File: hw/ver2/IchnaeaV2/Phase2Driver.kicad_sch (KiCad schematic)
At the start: 21 parts, among them Q2 MCAC80N10Y, Q3 MCAC80N10Y, Q4 MCAC80N10Y, Q5 MCAC80N10Y, U2 HIP2210

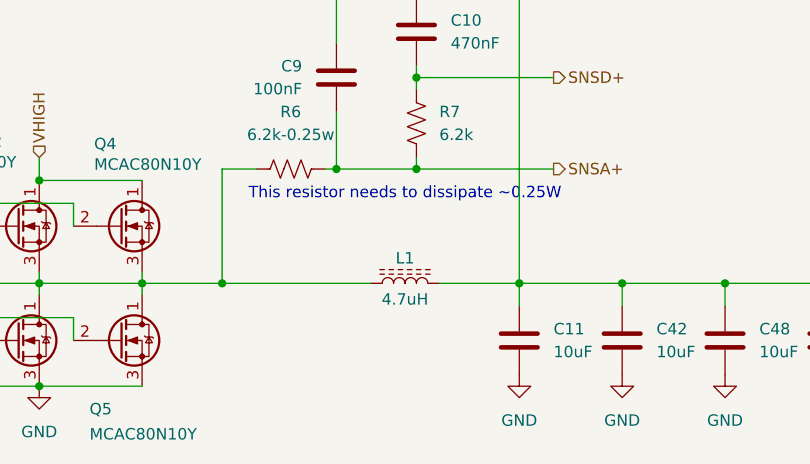
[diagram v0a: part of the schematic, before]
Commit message: Trying to optimize the high power loop area
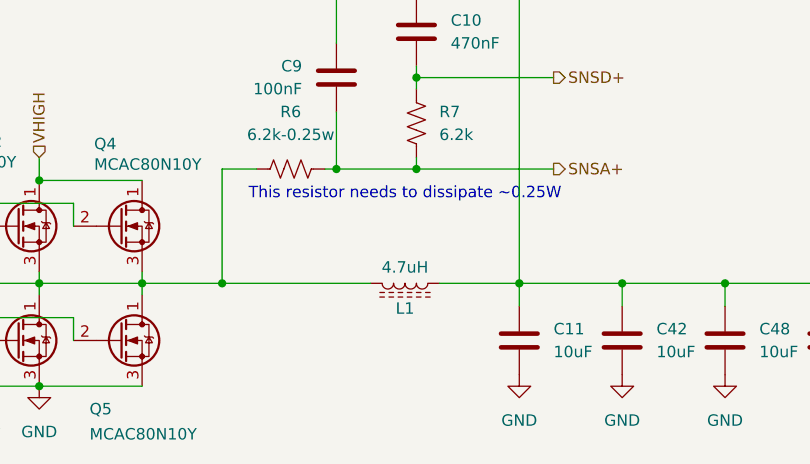
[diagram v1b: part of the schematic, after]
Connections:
- net SNSD-: now also L1.1; no longer L1.2
- net at C8.2, Q2.3 (S), Q3.1 (D)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: now also L1.2; no longer L1.1
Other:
- moved on the sheet: L1
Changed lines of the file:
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@@
 	(symbol
 		(lib_id "Device:L_Ferrite")
-		(at 203.2 95.25 90)
+		(at 203.2 95.25 270)
 		(unit 1)
 		(exclude_from_sim no)
@@
 		(dnp no)
 		(property "Reference" "L1"
-			(at 203.2 92.456 90)
+			(at 203.2 98.044 90)
 			(effects
 				(font
@@
 		)
 		(property "Value" "4.7uH"
-			(at 203.2 97.028 90)
+			(at 203.2 93.472 90)
 			(effects
 				(font
@@
 		)
 		(property "Digikey" "PQ2614BLA-3R3K-ND"
-			(at 203.708 99.06 90)
+			(at 202.692 91.44 90)
 			(effects
 				(font

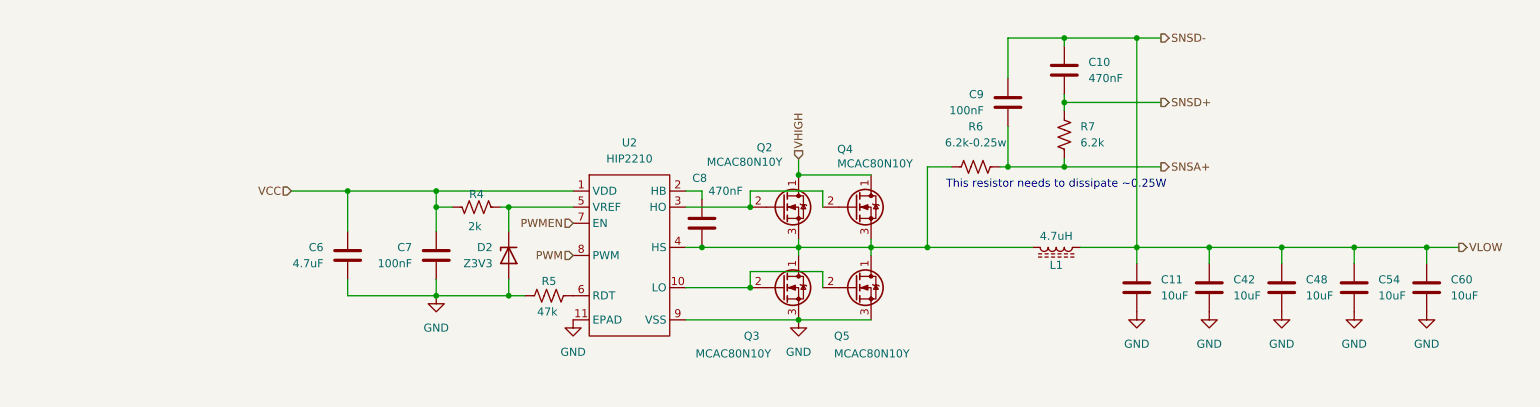
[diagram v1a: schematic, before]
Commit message: Trying to further compress power loop area
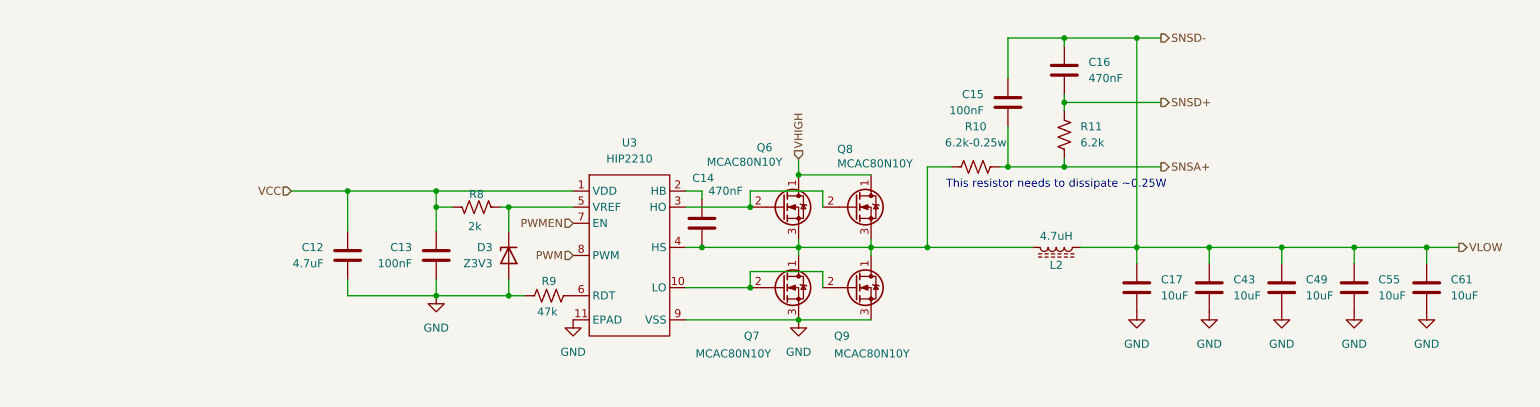
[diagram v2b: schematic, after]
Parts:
- renumbered C6 to C12, C7 to C13, C8 to C14, C9 to C15, C10 to C16, C11 to C17, C42 to C43, C48 to C49, C54 to C55, C60 to C61, D2 to D3, L1 to L2, Q2 to Q6, Q3 to Q7, Q4 to Q8, Q5 to Q9, R6 to R10, R7 to R11, R4 to R8, R5 to R9, U2 to U3

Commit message: Not quite happy with the power stage just yet.
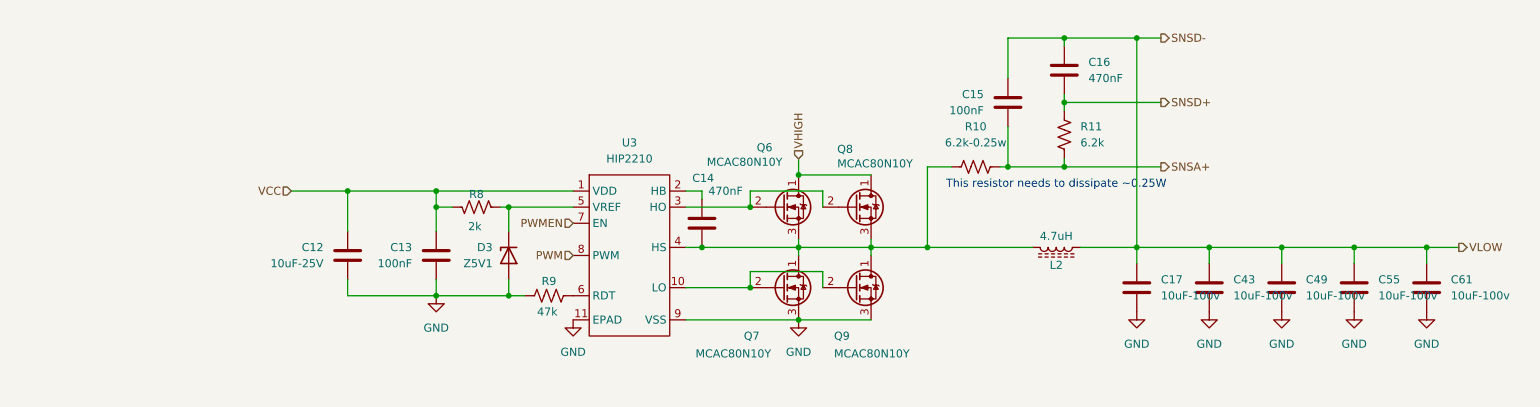
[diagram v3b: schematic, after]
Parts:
- C12: value 4.7uF -> 10uF-25V; LCSC C19666 -> C96446
- C17, C43, C49, C55, C61: value 10uF -> 10uF-100v
- D3: value Z3V3 -> Z5V1; LCSC C5353025 -> C2903912
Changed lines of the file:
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@@
 			)
 		)
-		(property "Value" "10uF"
+		(property "Value" "10uF-100v"
 			(at 242.57 102.8699 0)
 			(effects
@@
 			)
 		)
-		(property "Value" "4.7uF"
+		(property "Value" "10uF-25V"
 			(at 87.63 97.7899 0)
 			(effects
@@
 			)
 		)
-		(property "LCSC" "C19666"
+		(property "LCSC" "C96446"
 			(at 91.44 96.52 0)
 			(effects
@@
 			)
 		)
-		(property "Value" "10uF"
+		(property "Value" "10uF-100v"
 			(at 231.14 102.8699 0)
 			(effects
@@
 			)
 		)
-		(property "Value" "10uF"
+		(property "Value" "10uF-100v"
 			(at 219.71 102.8699 0)
 			(effects
@@
 			)
 		)
-		(property "Value" "Z3V3"
+		(property "Value" "Z5V1"
 			(at 114.3 97.7899 90)
 			(effects
@@
 			)
 		)
-		(property "LCSC" "C5353025"
+		(property "LCSC" "C2903912"
 			(at 116.84 96.52 90)
 			(effects
@@
 			)
 		)
-		(property "Value" "10uF"
+		(property "Value" "10uF-100v"
 			(at 254 102.8699 0)
 			(effects
@@
 			)
 		)
-		(property "Value" "10uF"
+		(property "Value" "10uF-100v"
 			(at 265.43 102.8699 0)
 			(effects

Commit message: Sync work to main PC
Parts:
- removed C13: 100nF, Capacitor_SMD:C_0603_1608Metric, symbol Device:C
- removed D3: Z5V1, Diode_SMD:D_SOD-123, symbol Device:D_Zener
- added C82, C83: 10uF-100v, Capacitor_SMD:C_1210_3225Metric_Pad1.33x2.70mm_HandSolder, symbol Device:C
- added R71: 0, Resistor_SMD:R_0603_1608Metric, symbol Device:R_US
- added R72: 10k, Resistor_SMD:R_0603_1608Metric, symbol Device:R_US
- added R73: 6.2k, Resistor_SMD:R_0603_1608Metric, symbol Device:R_US
- R8: value 2k -> 0; LCSC (none) -> C21189
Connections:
- net GND: now also C82.2, C83.2, R73.2
- net PWM: now also R71.2; no longer U3.8 (PWM)
- net PWMEN: now also R8.2; no longer U3.7 (EN)
- net SNSD-: now also L2.2; no longer L2.1
- net VCC: now also R72.1; no longer R8.2
- net VHIGH: now also C82.1, C83.1
- net at C14.2, Q6.3 (S), Q7.1 (D)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: now also L2.1; no longer L2.2
- net at R8.1: now also U3.7 (EN); no longer U3.5 (VREF)
- new net: R71.1, U3.8 (PWM)
- new net: R72.2, R73.1, U3.5 (VREF)
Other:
- moved on the sheet: C12, C14, C15, C16, C17, C43, C49, C55, C61, L2, Q6, Q7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

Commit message: More power stage layout
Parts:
- removed C49: 10uF-100v, Capacitor_SMD:C_1210_3225Metric_Pad1.33x2.70mm_HandSolder, symbol Device:C
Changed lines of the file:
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@@
-	)
-	(junction
-		(at 212.09 100.33)
-		(diameter 0)
-		(color 0 0 0 0)
 	)
 	(junction
@@
 	(wire
 		(pts
-			(xy 212.09 100.33) (xy 212.09 102.87)
-		)
-		(stroke
-			(width 0)
-			(type default)
-		)
-	)
-	(wire
-		(pts
 			(xy 189.23 67.31) (xy 177.8 67.31)
 		)
@@
 	(wire
 		(pts
-			(xy 212.09 100.33) (xy 223.52 100.33)
+			(xy 200.66 100.33) (xy 223.52 100.33)
 		)
 		(stroke
@@
 		(pts
 			(xy 92.71 93.98) (xy 102.87 93.98)
-		)
-		(stroke
-			(width 0)
-			(type default)
-		)
-	)
-	(wire
-		(pts
-			(xy 200.66 100.33) (xy 212.09 100.33)
 		)
 		(stroke
@@
 	)
 	(symbol
-		(lib_id "Device:C")
-		(at 212.09 106.68 0)
-		(unit 1)
-		(exclude_from_sim no)
-		(in_bom yes)
-		(on_board yes)
-		(dnp no)
-		(fields_autoplaced yes)
-		(property "Reference" "C49"
-			(at 215.9 105.4099 0)
-			(effects
-				(font
-					(size 1.27 1.27)
-				)
-				(justify left)
-			)
-		)
-		(property "Value" "10uF-100v"
-			(at 215.9 107.9499 0)
-			(effects
-				(font
-					(size 1.27 1.27)
-				)
-				(justify left)
-			)
-		)
-		(property "Footprint" "Capacitor_SMD:C_1210_3225Metric_Pad1.33x2.70mm_HandSolder"
-			(at 213.0552 110.49 0)
-			(effects
-				(font
-					(size 1.27 1.27)
-				)
-				(hide yes)
-			)
-		)
-		(property "Datasheet" "~"
-			(at 212.09 106.68 0)
-			(effects
-				(font
-					(size 1.27 1.27)
-				)
-				(hide yes)
-			)
-		)
-		(property "Description" "Unpolarized capacitor"
-			(at 212.09 106.68 0)
-			(effects
-				(font
-					(size 1.27 1.27)
-				)
-				(hide yes)
-			)
-		)
-		(property "Field-1" ""
-			(at 212.09 106.68 0)
-			(effects
-				(font
-					(size 1.27 1.27)
-				)
-				(hide yes)
-			)
-		)
-		(property "Digikey" "445-CGA6P1X7R1N106M250ACCT-ND"
-			(at 212.09 106.68 0)
-			(effects
-				(font
-					(size 1.27 1.27)
-				)
-				(hide yes)
-			)
-		)
-		(property "LCSC" "C576517"
-			(at 212.09 106.68 0)
-			(effects
-				(font
-					(size 1.27 1.27)
-				)
-				(hide yes)
-			)
-		)
-		(pin "1"
-		)
-		(pin "2"
-		)
-		(instances
-			(project "IchnaeaV2"
-				(path "/93408532-1ffa-463d-873c-16289d2b7987/31a930eb-86fc-490d-aa2b-31b72c4dd29d/acf0bc45-d506-42ae-8f5d-490b1286e5e0"
-					(reference "C49")
-					(unit 1)
-				)
-			)
-		)
-	)
-	(symbol
 		(lib_id "Device:L_Ferrite")
 		(at 176.53 100.33 90)
@@
 					(unit 1)
 				)
-			)
-		)
-	)
-	(symbol
-		(lib_id "power:GND")
-		(at 212.09 110.49 0)
-		(unit 1)
-		(exclude_from_sim no)
-		(in_bom yes)
-		(on_board yes)
-		(dnp no)
-		(fields_autoplaced yes)
-		(property "Reference" "#PWR075"
-			(at 212.09 116.84 0)
-			(effects
-				(font
-					(size 1.27 1.27)
-				)
-				(hide yes)
-			)
-		)
-		(property "Value" "GND"
-			(at 212.09 115.57 0)
-			(effects
-				(font
-					(size 1.27 1.27)
-				)
-			)
-		)
-		(property "Footprint" ""
-			(at 212.09 110.49 0)
-			(effects
-				(font
-					(size 1.27 1.27)
-				)
-				(hide yes)
-			)
-		)
-		(property "Datasheet" ""
-			(at 212.09 110.49 0)
-			(effects
-				(font
-					(size 1.27 1.27)
-				)
-				(hide yes)
-			)
-		)
-		(property "Description" "Power symbol creates a global label with name \"GND\" , ground"
-			(at 212.09 110.49 0)
-			(effects
-				(font
-					(size 1.27 1.27)
-				)
-				(hide yes)
-			)
-		)
-		(pin "1"
-		)
-		(instances
-			(project "IchnaeaV2"
-				(path "/93408532-1ffa-463d-873c-16289d2b7987/31a930eb-86fc-490d-aa2b-31b72c4dd29d/acf0bc45-d506-42ae-8f5d-490b1286e5e0"
-					(reference "#PWR075")
-					(unit 1)
-				)

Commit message: Partially work through the V1 notes. Start adding some of the control stage circuitry.
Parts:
- added TP19, TP20, TP21, TP22, TP23, TP49, TP50, TP51: TestPoint, TestPoint:TestPoint_Pad_D1.0mm, symbol Connector:TestPoint
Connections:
- net GND: now also TP23.1, TP51.1
- net PWM: now also TP20.1
- net PWMEN: now also TP19.1
- net SNSD-: now also TP50.1
- net at C14.2, L2.1, Q6.3 (S)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: now also TP49.1
- net at Q7.2 (G), Q9.2 (G), U3.10 (LO): now also TP21.1
- net at Q6.2 (G), Q8.2 (G), U3.3 (HO): now also TP22.1
